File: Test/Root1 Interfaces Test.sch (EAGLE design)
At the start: 12 parts, among them J1 1X5.SEI.AB, J2 1X10.SEI.AB, J3 1X5.SEI.AT.MATE, J4 1X10SEI.AT.MATE, U1 CAT24CXX.UDFN, U2 NC7S86.SC70-5

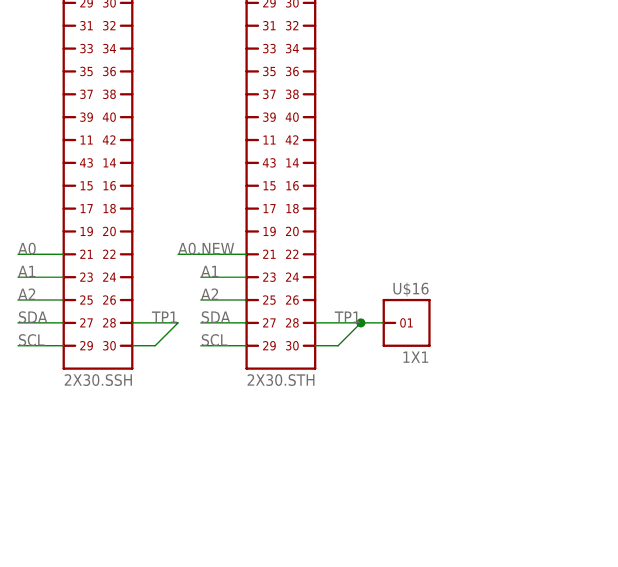
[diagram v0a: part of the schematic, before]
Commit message: Fixed routing issue in Root1 Interface Test PCB. EEPROM Address did not autoincrement...
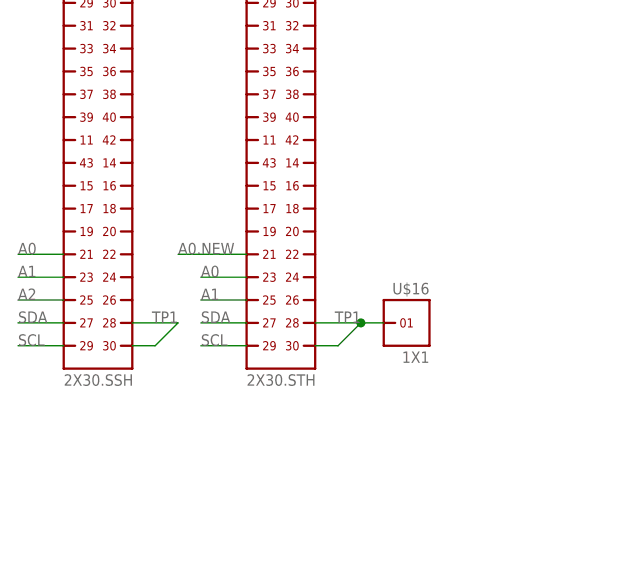
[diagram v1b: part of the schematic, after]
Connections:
- net A0: now also U$3.53
- net A1: now also U$3.55; no longer U$3.53
- net A2: no longer U$3.55
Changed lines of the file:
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@@
 <setting verticaltext="up"/>
 </settings>
-<grid distance="100" unitdist="mil" unit="mil" style="dots" multiple="1" display="yes" altdistance="25" altunitdist="mil" altunit="mil"/>
+<grid distance="0.1" unitdist="inch" unit="inch" style="lines" multiple="1" display="no" altdistance="0.01" altunitdist="inch" altunit="inch"/>
 <layers>
 <layer number="1" name="Top" color="4" fill="1" visible="no" active="no"/>
@@
 <label x="78.74" y="88.9" size="1.27" layer="95"/>
 </segment>
+<segment>
+<pinref part="U$3" gate="G$1" pin="53"/>
+<wire x1="99.06" y1="86.36" x2="104.14" y2="86.36" width="0.1524" layer="91"/>
+<label x="99.06" y="86.36" size="1.27" layer="95"/>
+</segment>
 </net>
 <net name="A1" class="0">
@@
 </segment>
 <segment>
-<pinref part="U$3" gate="G$1" pin="53"/>
-<wire x1="99.06" y1="86.36" x2="104.14" y2="86.36" width="0.1524" layer="91"/>
-<label x="99.06" y="86.36" size="1.27" layer="95"/>
-</segment>
-<segment>
 <pinref part="U$2" gate="G$1" pin="53"/>
 <wire x1="83.82" y1="86.36" x2="78.74" y2="86.36" width="0.1524" layer="91"/>
 <label x="78.74" y="86.36" size="1.27" layer="95"/>
 </segment>
+<segment>
+<pinref part="U$3" gate="G$1" pin="55"/>
+<wire x1="104.14" y1="83.82" x2="99.06" y2="83.82" width="0.1524" layer="91"/>
+<label x="99.06" y="83.82" size="1.27" layer="95"/>
+</segment>
 </net>
 <net name="A2" class="0">
@@
 </segment>
 <segment>
-<pinref part="U$3" gate="G$1" pin="55"/>
-<wire x1="104.14" y1="83.82" x2="99.06" y2="83.82" width="0.1524" layer="91"/>
-<label x="99.06" y="83.82" size="1.27" layer="95"/>
-</segment>
-<segment>
